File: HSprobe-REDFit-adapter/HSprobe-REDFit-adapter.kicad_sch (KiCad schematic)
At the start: 7 parts, among them J1 Conn_02x10_Odd_Even, J2 Conn_02x10_Odd_Even, J3 uart_host_2.54, SW1 Reset

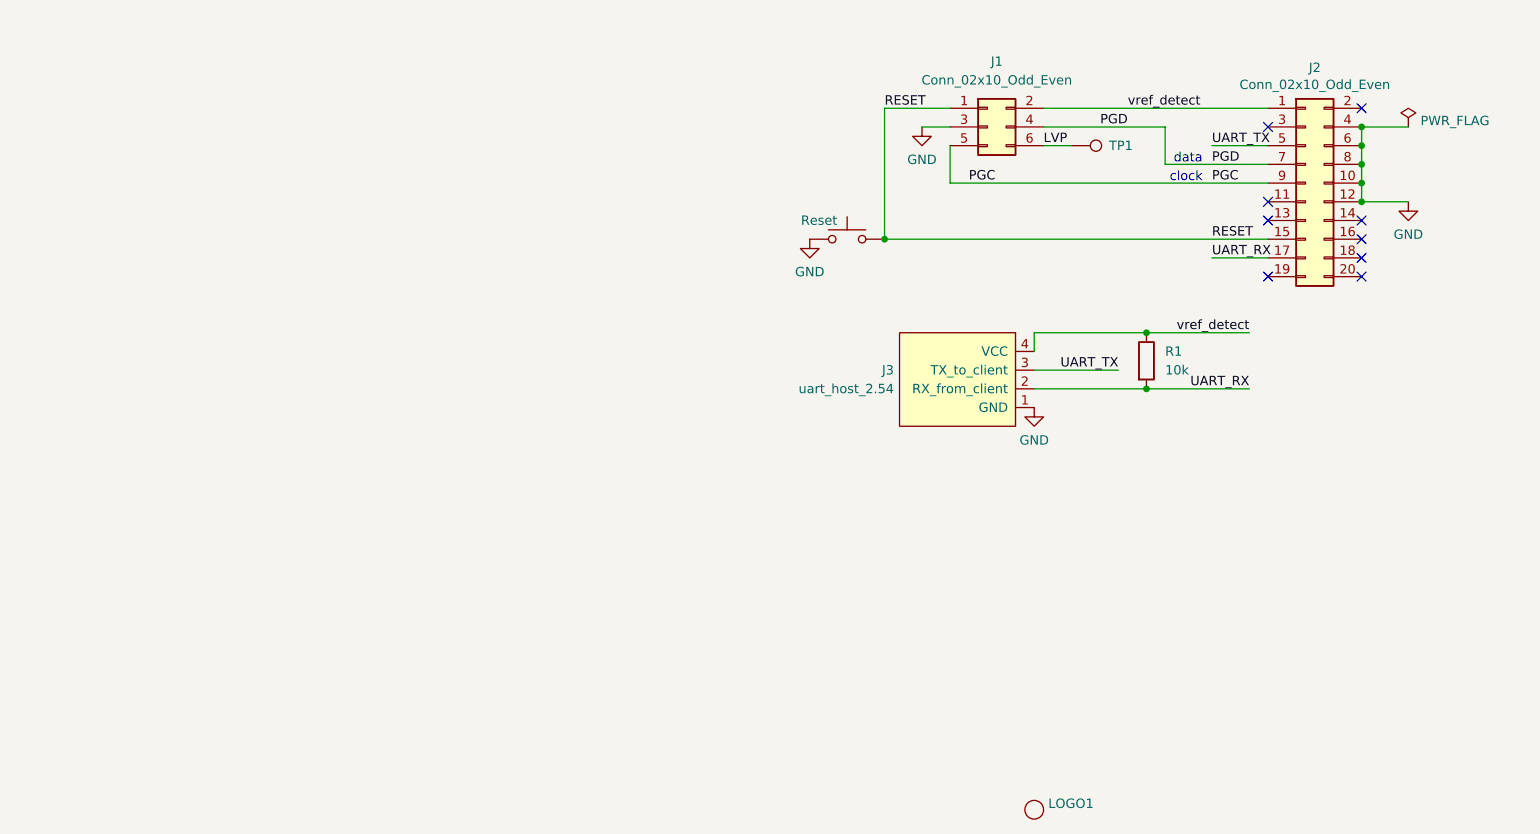
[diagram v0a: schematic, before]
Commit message: Modernize the adapter boards
This repo contains adapter boards for the Jitter 6-pins REDFit debug
interface to multiple standard programming/debug tools.
Each now renamed to make this clearer (BMP/HSProbe/JLink) and save those
projects as modern Kicad10 designs
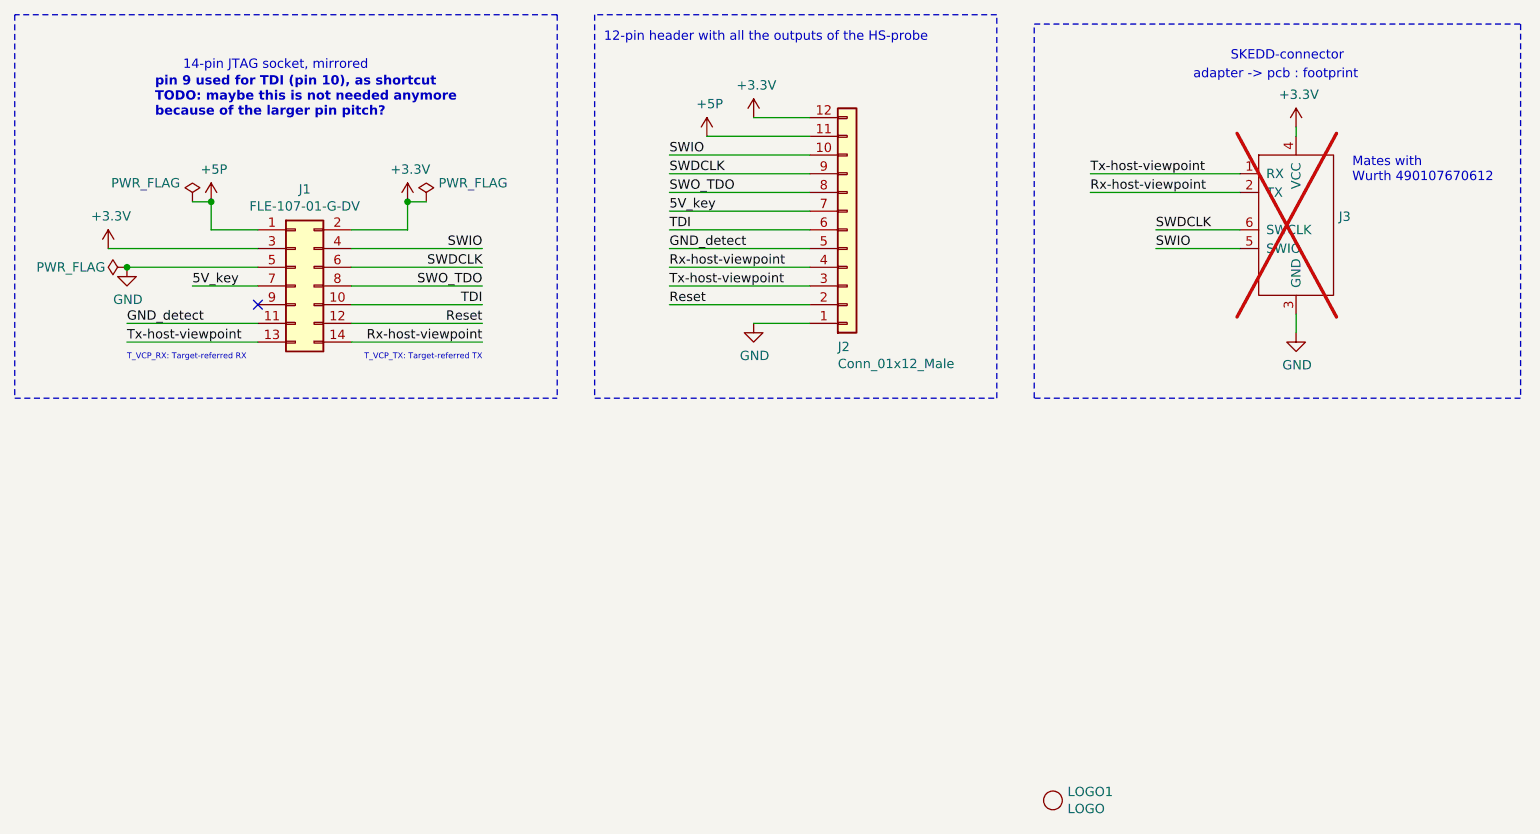
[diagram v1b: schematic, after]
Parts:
- removed J1: Conn_02x10_Odd_Even, Connector_IDC:IDC-Header_2x03_P2.54mm_Vertical, symbol Connector_Generic:Conn_02x03_Odd_Even
- removed J2: Conn_02x10_Odd_Even, Jitter_Connectors:JLink_PinHeader_2x10_2.54_Horizontal, symbol Connector_Generic:Conn_02x10_Odd_Even
- removed J3: uart_host_2.54, Connector_PinHeader_2.54mm:PinHeader_1x04_P2.54mm_Vertical, symbol Jitter_Components:uart_host_2.54
- removed R1: 10k, Resistor_SMD:R_0603_1608Metric, symbol Device:R
- removed SW1: Reset, Button_Switch_SMD:SW_SPST_EVQPE1, symbol Switch:SW_Push
- removed TP1: TestPoint, TestPoint:TestPoint_THTPad_D1.0mm_Drill0.5mm, symbol Connector:TestPoint
- added J1: FLE-107-01-G-DV, Connector_PinSocket_1.27mm:PinSocket_2x07_P1.27mm_Vertical_SMD, symbol Connector_Generic:Conn_02x07_Odd_Even
- added J2: Conn_01x12_Male, Connector_PinHeader_2.54mm:PinHeader_2x06_P2.54mm_Vertical, symbol Connector_Generic:Conn_01x12
- added J3: DNI, Jitter_Footprints:WR-WST_REDFIT-6-pins_490107670612-adapter_to_pcb, symbol Jitter_Components:swd_with_uart_client
- LOGO1: footprint Jitter_Logos:JitterLogo -> Jitter_Logos:Jitter-mini
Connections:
- net GND: now also J1.5 (Pin_5), J2.1 (Pin_1), J3.3 (GND)
- new net +3.3V: J1.2 (Pin_2), J1.3 (Pin_3), J2.12 (Pin_12), J3.4 (VCC)
- new net +5P: J1.1 (Pin_1), J2.11 (Pin_11)
- new net 5V_key: J1.7 (Pin_7), J2.7 (Pin_7)
- new net GND_detect: J1.11 (Pin_11), J2.5 (Pin_5)
- new net Reset: J1.12 (Pin_12), J2.2 (Pin_2)
- new net Rx-host-viewpoint: J1.14 (Pin_14), J2.4 (Pin_4), J3.2 (TX)
- new net SWDCLK: J1.6 (Pin_6), J2.9 (Pin_9), J3.6 (SWCLK)
- new net SWIO: J1.4 (Pin_4), J2.10 (Pin_10), J3.5 (SWIO)
- new net SWO_TDO: J1.8 (Pin_8), J2.8 (Pin_8)
- new net TDI: J1.10 (Pin_10), J2.6 (Pin_6)
- new net Tx-host-viewpoint: J1.13 (Pin_13), J2.3 (Pin_3), J3.1 (RX)
- no-connect marks 9 -> 1
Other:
- note added: "12-pin header with all the outputs of the HS-probe"
- note added: "14-pin JTAG socket, mirrored"
- note added: "Mates with Wurth 490107670612"
- note added: "SKEDD-connector"
- note added: "T_VCP_RX: Target-referred RX"
- note added: "T_VCP_TX: Target-referred TX"
- note added: "adapter -> pcb : footprint"
- note added: "pin 9 used for TDI (pin 10), as shortcut TODO: maybe this is not needed anymore because of the larger pin pitch?"
- note removed: "clock"
- note removed: "data"
- company: Jitter -> (none)
- title: Jlink to TC2030-IDC__microchip adapter -> HSprobe-REDFit adapter
